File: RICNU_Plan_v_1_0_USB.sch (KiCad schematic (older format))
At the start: 15 parts, among them J1 USB_OTG, Q1 N-CH

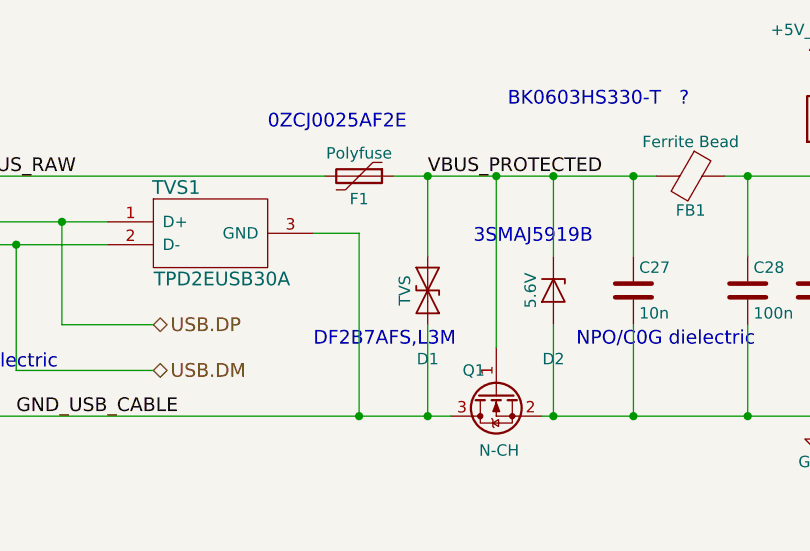
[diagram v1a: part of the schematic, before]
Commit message: Added connections to monitor power, changed CANSTB MCU pin, moved LED pins around
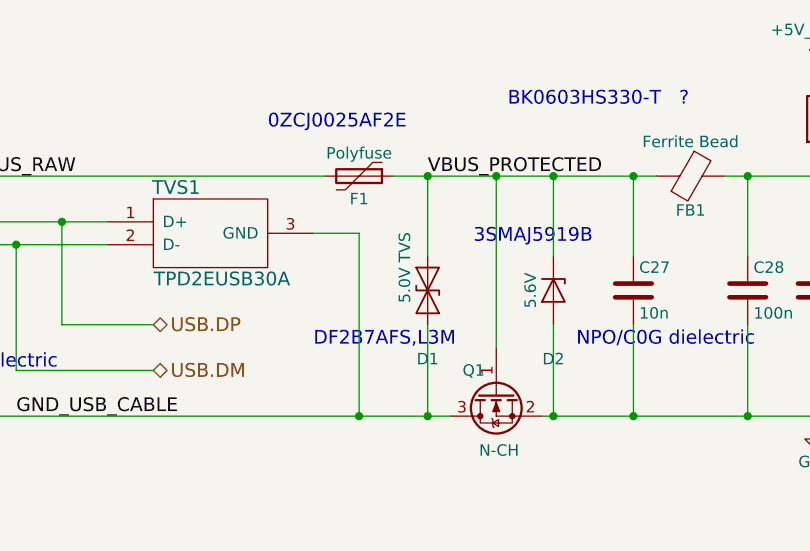
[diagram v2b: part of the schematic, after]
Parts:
- D1: value TVS -> 5.0V TVS
- FB1: footprint Resistors_SMD:R_0603_HandSoldering -> Resistors_SMD:R_0402_NoSilk
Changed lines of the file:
@@
 $EndComp
 $Comp
-L GND #PWR057
+L GND #PWR058
 U 1 1 5A024F9B
 P 8000 4700
-F 0 "#PWR057" H 8000 4450 50  0001 C CNN
+F 0 "#PWR058" H 8000 4450 50  0001 C CNN
 F 1 "GND" H 8000 4550 50  0000 C CNN
 F 2 "" H 8000 4700 50  0001 C CNN
@@
 P 6300 4100
 F 0 "D1" V 6600 4100 50  0000 C CNN
-F 1 "TVS" H 6300 4000 50  0000 C CNN
+F 1 "5.0V TVS" H 6200 4000 50  0000 C CNN
 F 2 "Diodes_SMD:D_SOD-523" H 6300 4100 50  0001 C CNN
 F 3 "" H 6300 4100 50  0001 C CNN
@@
 F 0 "FB1" V 7600 3600 50  0000 C CNN
 F 1 "Ferrite Bead" V 7300 3600 50  0000 C CNN
-F 2 "Resistors_SMD:R_0603_HandSoldering" V 7380 3600 50  0001 C CNN
+F 2 "Resistors_SMD:R_0402_NoSilk" V 7380 3600 50  0001 C CNN
 F 3 "" H 7450 3600 50  0001 C CNN
 	1    7450 3600
@@
 $EndComp
 $Comp
-L +5V_USB #PWR058
+L +5V_USB #PWR059
 U 1 1 5A02502A
 P 4100 3100
-F 0 "#PWR058" H 4100 2950 50  0001 C CNN
+F 0 "#PWR059" H 4100 2950 50  0001 C CNN
 F 1 "+5V_USB" H 4100 3240 50  0000 C CNN
 F 2 "" H 4100 3100 50  0001 C CNN
@@
 $EndComp
 $Comp
-L +5V_USB_P #PWR059
+L +5V_USB_P #PWR060
 U 1 1 5A025030
 P 8000 3100
-F 0 "#PWR059" H 8000 2950 50  0001 C CNN
+F 0 "#PWR060" H 8000 2950 50  0001 C CNN
 F 1 "+5V_USB_P" H 8000 3240 50  0000 C CNN
 F 2 "" H 8000 3100 50  0001 C CNN
@@
 Connection ~ 6600 3600
 $Comp
-L PWR_FLAG #FLG060
+L PWR_FLAG #FLG061
 U 1 1 59FD35E0
 P 3350 4700
-F 0 "#FLG060" H 3350 4775 50  0001 C CNN
+F 0 "#FLG061" H 3350 4775 50  0001 C CNN
 F 1 "PWR_FLAG" H 3350 4850 50  0000 C CNN
 F 2 "" H 3350 4700 50  0001 C CNN

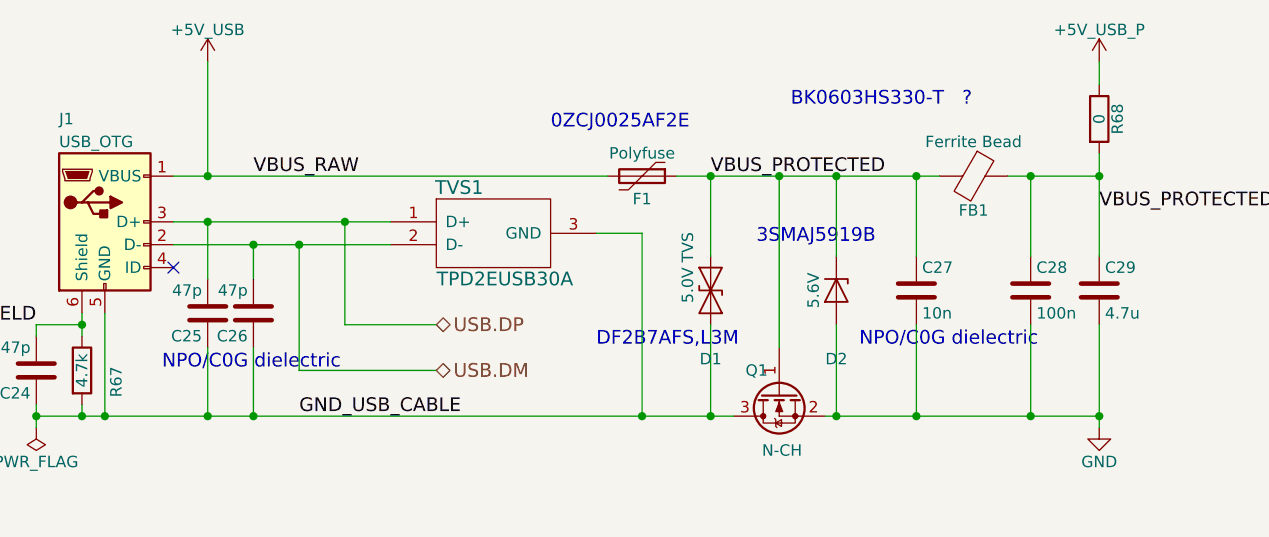
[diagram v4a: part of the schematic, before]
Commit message: Various small changes like comment removal
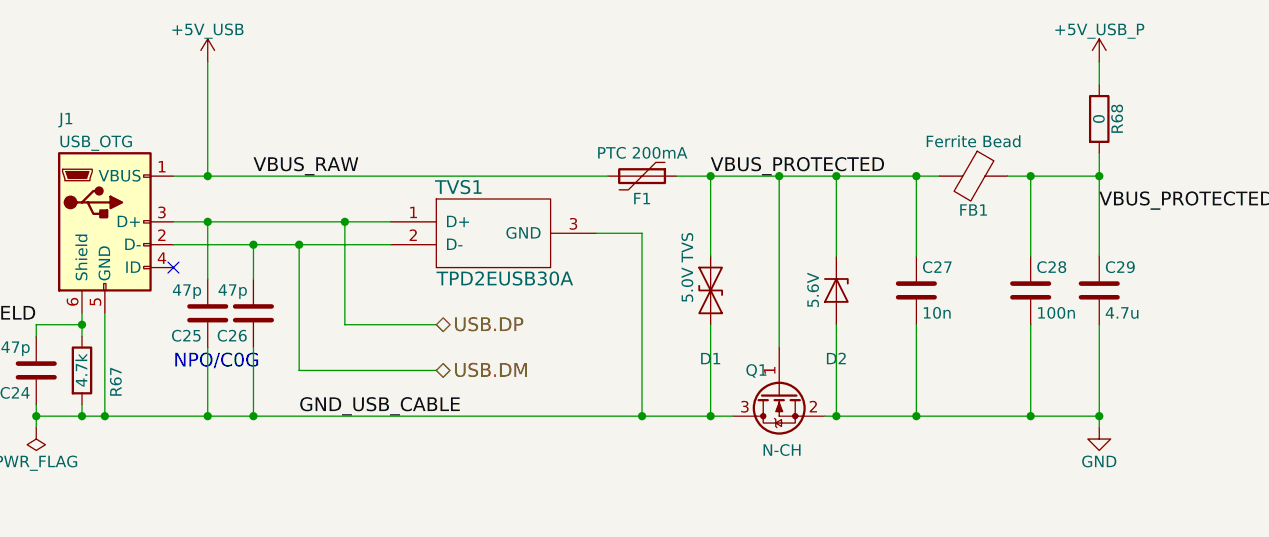
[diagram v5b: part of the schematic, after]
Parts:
- F1: value Polyfuse -> PTC 200mA
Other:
- note added: "NPO/C0G"
- note removed: "0ZCJ0025AF2E"
- note removed: "3SMAJ5919B"
- note removed: "?"
- note removed: "BK0603HS330-T"
- note removed: "DF2B7AFS,L3M"
- note removed: "NPO/C0G dielectric"
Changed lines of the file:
@@
 P 6000 3600
 F 0 "F1" V 6100 3600 50  0000 C CNN
-F 1 "Polyfuse" V 5900 3600 50  0000 C CNN
+F 1 "PTC 200mA" V 5900 3600 50  0000 C CNN
 F 2 "Resistors_SMD:R_0603_HandSoldering" H 6050 3400 50  0001 L CNN
 F 3 "" H 6000 3600 50  0001 C CNN
@@
 	1    0    0    -1
 $EndComp
-Text Notes 6500 3900 0    60   ~ 0
-3SMAJ5919B
-Text Notes 5800 4350 0    60   ~ 0
-DF2B7AFS,L3M
-Text Notes 5600 3400 0    60   ~ 0
-0ZCJ0025AF2E
 Wire Wire Line
 	3550 4200 3550 4300
@@
 	6000 3850 6000 4650
 Connection ~ 6000 4650
-Text Notes 6950 4350 0    60   ~ 0
-NPO/C0G dielectric
-Text Notes 7400 3300 0    60   ~ 0
-?
-Text Notes 6650 3300 0    60   ~ 0
-BK0603HS330-T
-Text Notes 3900 4450 0    60   ~ 0
-NPO/C0G dielectric
 Wire Wire Line
 	3350 4600 3350 4700
@@
 Text Label 3350 4250 2    60   ~ 0
 USB_SHIELD
+Text Notes 3950 4450 0    60   ~ 0
+NPO/C0G
 $EndSCHEMATC

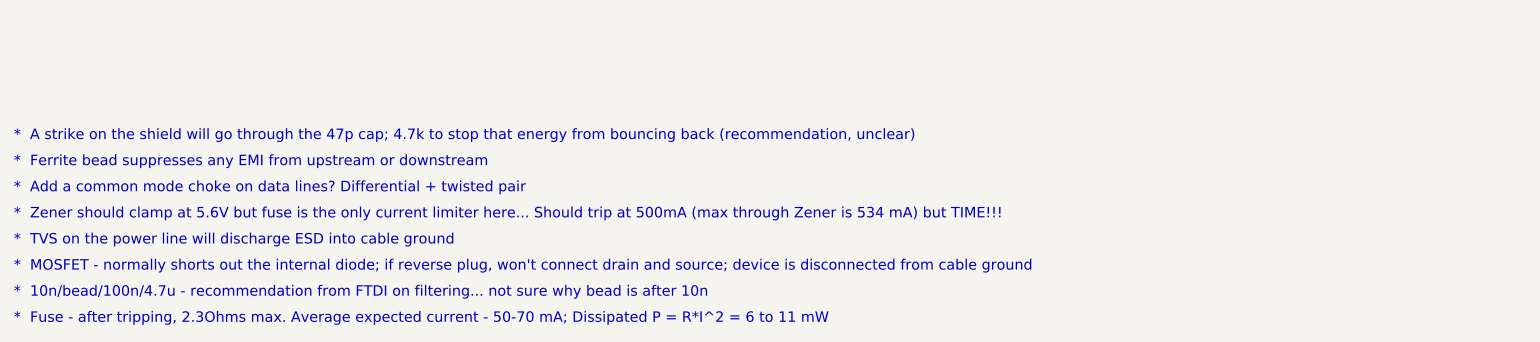
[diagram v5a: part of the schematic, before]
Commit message: Deleting PDFs
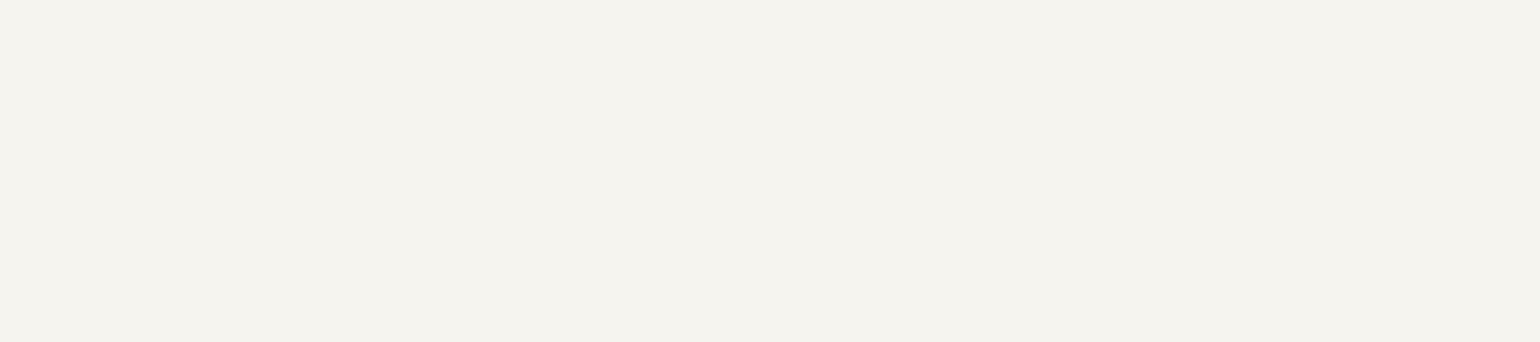
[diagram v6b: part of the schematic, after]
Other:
- note removed: "* 10n/bead/100n/4.7u - recommendation from FTDI on filtering... not sure why bead is after 10n"
- note removed: "* A strike on the shield will go through the 47p cap; 4.7k to stop that energy from bouncing back (recommendation, unclear)"
- note removed: "* Add a common mode choke on data lines? Differential + twisted pair"
- note removed: "* Ferrite bead suppresses any EMI from upstream or downstream"
- note removed: "* Fuse - after tripping, 2.3Ohms max. Average expected current - 50-70 mA; Dissipated P = R*I^2 = 6 to 11 mW"
- note removed: "* MOSFET - normally shorts out the internal diode; if reverse plug, won't connect drain and source; device is disconnected from cable ground"
- note removed: "* TVS on the power line will discharge ESD into cable ground"
- note removed: "* Zener should clamp at 5.6V but fuse is the only current limiter here... Should trip at 500mA (max through Zener is 534 mA) but TIME!!!"
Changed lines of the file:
@@
 	-1   0    0    1
 $EndComp
-Text Notes 150  8800 0    60   ~ 0
-*  A strike on the shield will go through the 47p cap; 4.7k to stop that energy from bouncing back (recommendation, unclear)
-Text Notes 150  8950 0    60   ~ 0
-*  Ferrite bead suppresses any EMI from upstream or downstream
-Text Notes 150  9100 0    60   ~ 0
-*  Add a common mode choke on data lines? Differential + twisted pair
-Text Notes 150  9250 0    60   ~ 0
-*  Zener should clamp at 5.6V but fuse is the only current limiter here... Should trip at 500mA (max through Zener is 534 mA) but TIME!!!
-Text Notes 150  9400 0    60   ~ 0
-*  TVS on the power line will discharge ESD into cable ground
-Text Notes 150  9550 0    60   ~ 0
-*  MOSFET - normally shorts out the internal diode; if reverse plug, won't connect drain and source; device is disconnected from cable ground
-Text Notes 150  9700 0    60   ~ 0
-*  10n/bead/100n/4.7u - recommendation from FTDI on filtering... not sure why bead is after 10n
-Text Notes 150  9850 0    60   ~ 0
-*  Fuse - after tripping, 2.3Ohms max. Average expected current - 50-70 mA; Dissipated P = R*I^2 = 6 to 11 mW
 Text Label 4500 4650 0    60   ~ 0
 GND_USB_CABLE
